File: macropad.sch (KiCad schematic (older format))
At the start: 27 parts

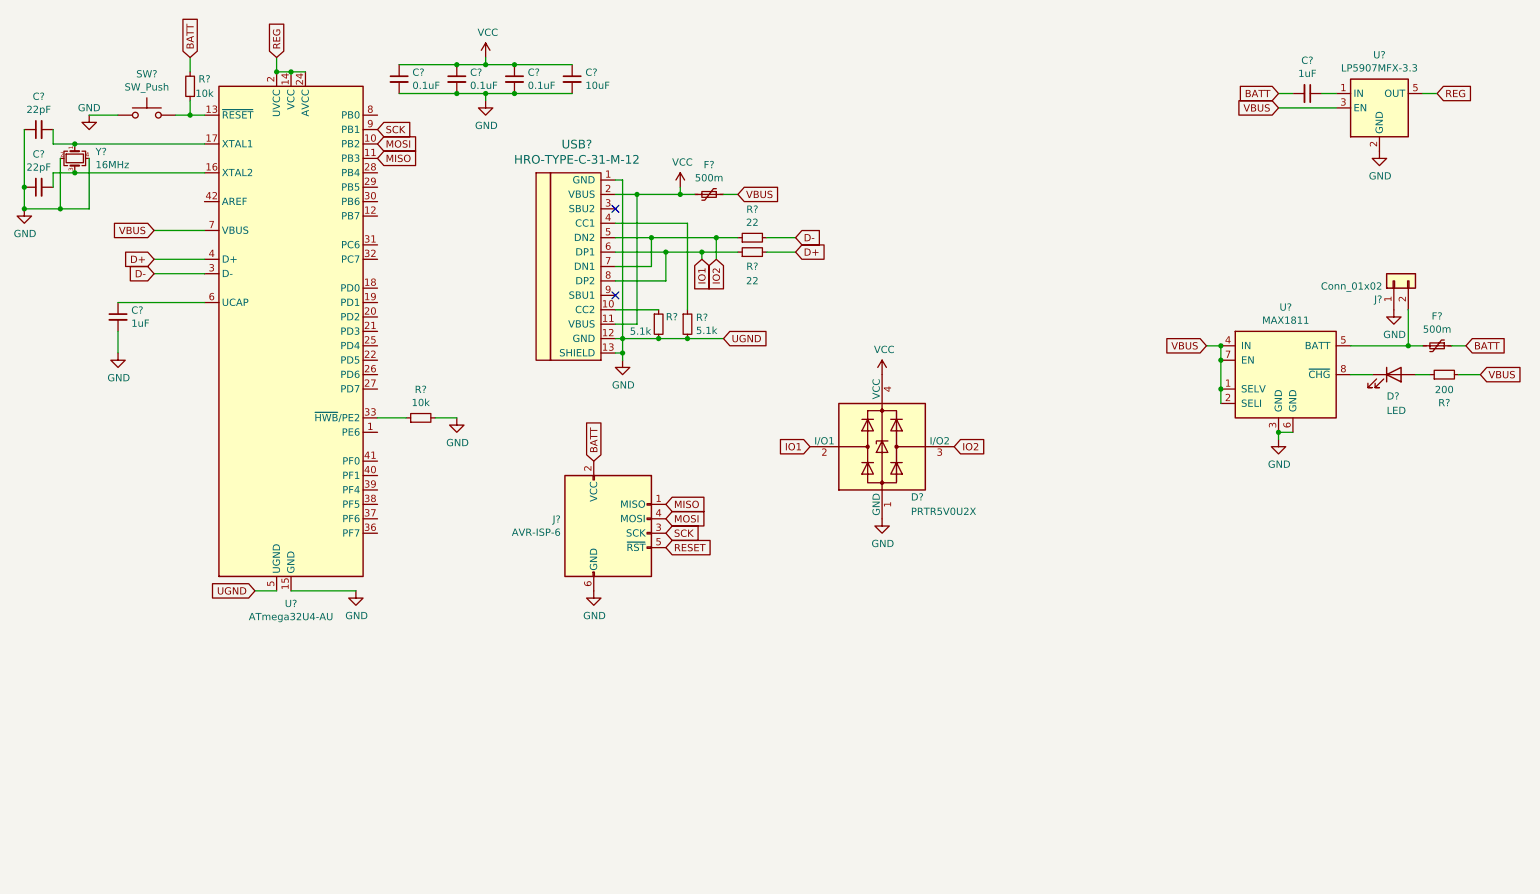
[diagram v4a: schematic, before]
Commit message: Power source switching, hopefully it doesn't explode
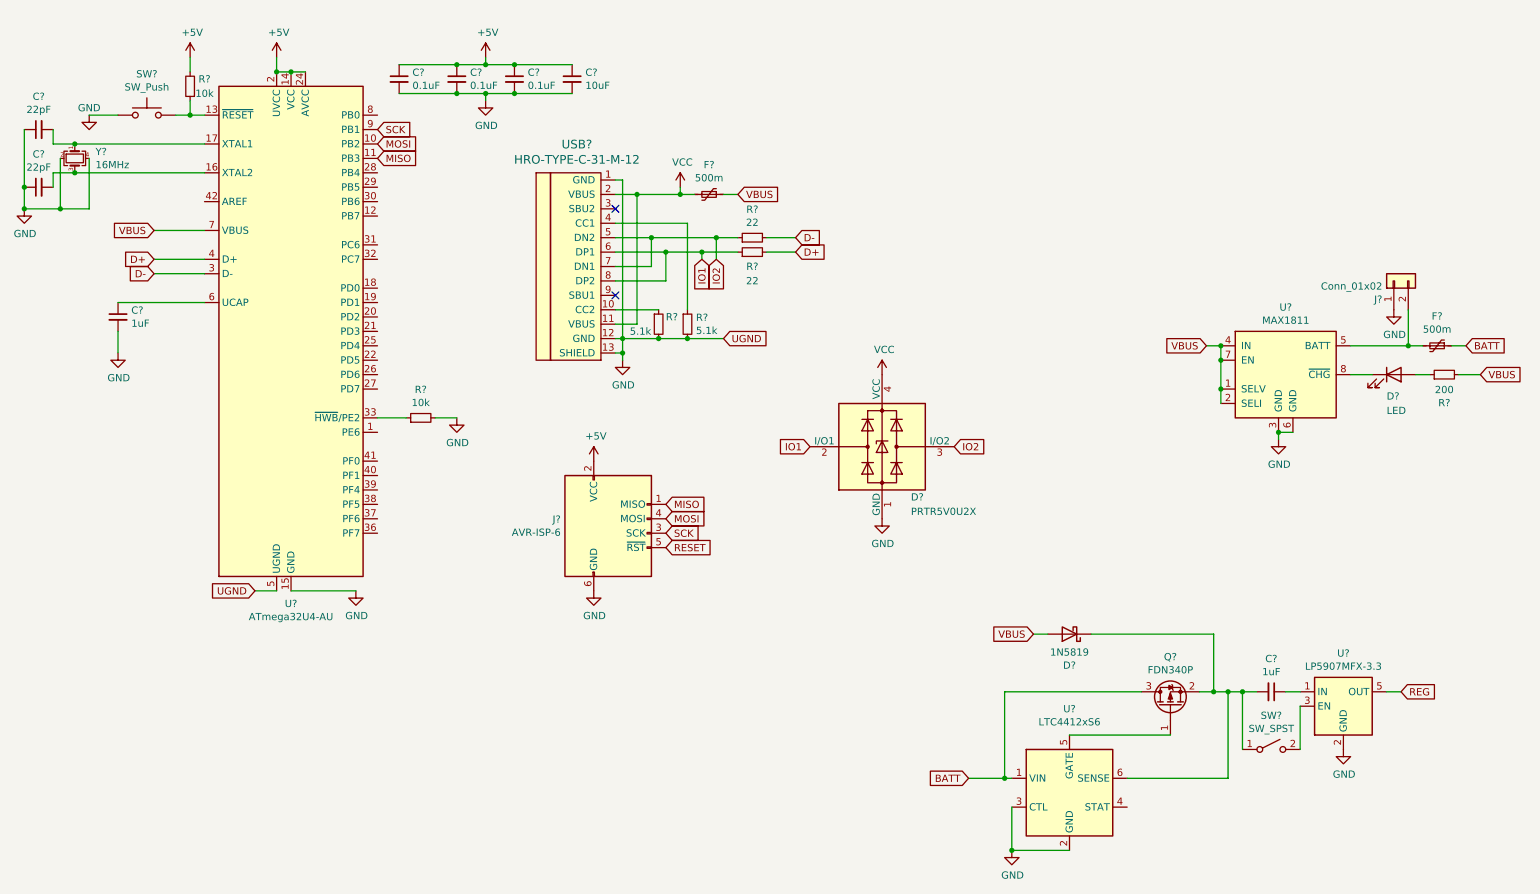
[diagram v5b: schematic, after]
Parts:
- added D?: 1N5819, Diode_THT:D_DO-41_SOD81_P10.16mm_Horizontal, symbol Diode:1N5819
- added Q?: FDN340P, Package_TO_SOT_SMD:SOT-23, symbol Transistor_FET:FDN340P
- added SW?: SW_SPST, symbol Switch:SW_SPST
- added U?: LTC4412xS6, Package_TO_SOT_SMD:TSOT-23-6, symbol Power_Management:LTC4412xS6
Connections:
- net BATT: now also Q?.3 (D), U?.1 (VIN); no longer C?.2, J?.2 (VCC), R?.2
- net GND: now also U?.2 (GND), U?.3 (CTL)
- net REG: no longer U?.14 (VCC), U?.2 (UVCC), U?.24 (AVCC), U?.34 (VCC), U?.44 (AVCC)
- net VBUS: now also D?.2 (A); no longer U?.3 (EN)
- net VCC: no longer C?.1, C?.1, C?.1, C?.1
- new net: SW?.2 (B), U?.3 (EN)
- new net: C?.2, D?.1 (K), Q?.2 (S), SW?.1 (A), U?.6 (SENSE)
- new net: Q?.1 (G), U?.5 (GATE)
- new net +5V: C?.1, C?.1, C?.1, C?.1, J?.2 (VCC), R?.2, U?.14 (VCC), U?.2 (UVCC), U?.24 (AVCC), U?.34 (VCC), U?.44 (AVCC)
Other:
- moved on the sheet: C?, U?
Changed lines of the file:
@@
 	1000 1550 1900 1550
-Wire Wire Line
-	3850 800  4050 800
-Connection ~ 3850 800
-Wire Wire Line
-	3650 800  3850 800
 Wire Wire Line
 	3650 1000 3850 1000
@@
 Wire Wire Line
 	3850 1050 3850 1000
-Wire Wire Line
-	3850 750  3850 800
-$Comp
-L power:VCC #PWR?
-U 1 1 60C49678
-P 3850 750
-F 0 "#PWR?" H 3850 600 50  0001 C CNN
-F 1 "VCC" H 3865 923 50  0000 C CNN
-F 2 "" H 3850 750 50  0001 C CNN
-F 3 "" H 3850 750 50  0001 C CNN
-	1    3850 750
-	1    0    0    -1
-$EndComp
 $Comp
 L Device:C_Small C?
@@
 Text GLabel 5500 2700 2    50   Input ~ 0
 UGND
-Text GLabel 2400 750  1    50   Input ~ 0
-REG
 $Comp
 L Device:R_Small R?
@@
 L Regulator_Linear:LP5907MFX-3.3 U?
 U 1 1 60D4DF09
-P 10050 1100
-F 0 "U?" H 10050 1467 50  0000 C CNN
-F 1 "LP5907MFX-3.3" H 10050 1376 50  0000 C CNN
-F 2 "Package_TO_SOT_SMD:SOT-23-5" H 10050 1450 50  0001 C CNN
-F 3 "http://www.ti.com/lit/ds/symlink/lp5907.pdf" H 10050 1600 50  0001 C CNN
-	1    10050 1100
-	1    0    0    -1
-$EndComp
-Text GLabel 9350 1000 0    50   Input ~ 0
-BATT
-Wire Wire Line
-	9650 1000 9750 1000
+P 9800 5250
+F 0 "U?" H 9800 5617 50  0000 C CNN
+F 1 "LP5907MFX-3.3" H 9800 5526 50  0000 C CNN
+F 2 "Package_TO_SOT_SMD:SOT-23-5" H 9800 5600 50  0001 C CNN
+F 3 "http://www.ti.com/lit/ds/symlink/lp5907.pdf" H 9800 5750 50  0001 C CNN
+	1    9800 5250
+	1    0    0    -1
+$EndComp
+Wire Wire Line
+	9400 5150 9500 5150
 $Comp
 L Device:C_Small C?
 U 1 1 60D5BC90
-P 9550 1000
-F 0 "C?" V 9321 1000 50  0000 C CNN
-F 1 "1uF" V 9412 1000 50  0000 C CNN
-F 2 "" H 9550 1000 50  0001 C CNN
-F 3 "~" H 9550 1000 50  0001 C CNN
-	1    9550 1000
+P 9300 5150
+F 0 "C?" V 9071 5150 50  0000 C CNN
+F 1 "1uF" V 9162 5150 50  0000 C CNN
+F 2 "" H 9300 5150 50  0001 C CNN
+F 3 "~" H 9300 5150 50  0001 C CNN
+	1    9300 5150
 	0    1    1    0
 $EndComp
-Wire Wire Line
-	9350 1000 9450 1000
 $Comp
 L power:GND #PWR?
 U 1 1 60D69A13
-P 10050 1400
-F 0 "#PWR?" H 10050 1150 50  0001 C CNN
-F 1 "GND" H 10055 1227 50  0000 C CNN
-F 2 "" H 10050 1400 50  0001 C CNN
-F 3 "" H 10050 1400 50  0001 C CNN
-	1    10050 1400
-	1    0    0    -1
-$EndComp
-Text GLabel 9350 1100 0    50   Input ~ 0
-VBUS
-Wire Wire Line
-	9350 1100 9750 1100
-Text GLabel 10450 1000 2    50   Input ~ 0
+P 9800 5550
+F 0 "#PWR?" H 9800 5300 50  0001 C CNN
+F 1 "GND" H 9805 5377 50  0000 C CNN
+F 2 "" H 9800 5550 50  0001 C CNN
+F 3 "" H 9800 5550 50  0001 C CNN
+	1    9800 5550
+	1    0    0    -1
+$EndComp
+Text GLabel 10200 5150 2    50   Input ~ 0
 REG
 Wire Wire Line
-	10450 1000 10350 1000
+	10200 5150 10100 5150
 $Comp
 L Battery_Management:MAX1811 U?
@@
 Text GLabel 5100 4150 2    50   Input ~ 0
 RESET
-Text GLabel 4600 3550 1    50   Input ~ 0
-BATT
 $Comp
 L power:GND #PWR?
@@
 Wire Wire Line
 	1700 1150 1800 1150
-Text GLabel 1800 750  1    50   Input ~ 0
-BATT
 Wire Wire Line
 	1800 750  1800 850
@@
 	-1   0    0    1
 $EndComp
+$Comp
+L Power_Management:LTC4412xS6 U?
+U 1 1 60FD7D97
+P 7900 5850
+F 0 "U?" H 7900 6431 50  0000 C CNN
+F 1 "LTC4412xS6" H 7900 6340 50  0000 C CNN
+F 2 "Package_TO_SOT_SMD:TSOT-23-6" H 8550 5500 50  0001 C CNN
+F 3 "https://www.analog.com/media/en/technical-documentation/data-sheets/4412fb.pdf" H 10000 5650 50  0001 C CNN
+	1    7900 5850
+	1    0    0    -1
+$EndComp
+$Comp
+L Diode:1N5819 D?
+U 1 1 60FF6140
+P 7900 4750
+F 0 "D?" H 7900 4967 50  0000 C CNN
+F 1 "1N5819" H 7900 4876 50  0000 C CNN
+F 2 "Diode_THT:D_DO-41_SOD81_P10.16mm_Horizontal" H 7900 4575 50  0001 C CNN
+F 3 "http://www.vishay.com/docs/88525/1n5817.pdf" H 7900 4750 50  0001 C CNN
+	1    7900 4750
+	-1   0    0    1
+$EndComp
+Wire Wire Line
+	3650 800  3850 800
+Wire Wire Line
+	3850 800  3850 750
+Connection ~ 3850 800
+Wire Wire Line
+	3850 800  4050 800
+$Comp
+L Transistor_FET:FDN340P Q?
+U 1 1 610158B0
+P 8600 5250
+F 0 "Q?" V 8942 5250 50  0000 C CNN
+F 1 "FDN340P" V 8851 5250 50  0000 C CNN
+F 2 "Package_TO_SOT_SMD:SOT-23" H 8800 5175 50  0001 L CIN
+F 3 "https://www.onsemi.com/pub/Collateral/FDN340P-D.PDF" H 8600 5250 50  0001 L CNN
+	1    8600 5250
+	0    -1   -1   0
+$EndComp
+$Comp
+L power:+5V #PWR?
+U 1 1 61021E90
+P 2400 750
+F 0 "#PWR?" H 2400 600 50  0001 C CNN
+F 1 "+5V" H 2415 923 50  0000 C CNN
+F 2 "" H 2400 750 50  0001 C CNN
+F 3 "" H 2400 750 50  0001 C CNN
+	1    2400 750
+	1    0    0    -1
+$EndComp
+$Comp
+L power:+5V #PWR?
+U 1 1 610232C4
+P 1800 750
+F 0 "#PWR?" H 1800 600 50  0001 C CNN
+F 1 "+5V" H 1815 923 50  0000 C CNN
+F 2 "" H 1800 750 50  0001 C CNN
+F 3 "" H 1800 750 50  0001 C CNN
+	1    1800 750
+	1    0    0    -1
+$EndComp
+$Comp
+L power:+5V #PWR?
+U 1 1 610277FD
+P 4600 3550
+F 0 "#PWR?" H 4600 3400 50  0001 C CNN
+F 1 "+5V" H 4615 3723 50  0000 C CNN
+F 2 "" H 4600 3550 50  0001 C CNN
+F 3 "" H 4600 3550 50  0001 C CNN
+	1    4600 3550
+	1    0    0    -1
+$EndComp
+$Comp
+L power:+5V #PWR?
+U 1 1 610420AE
+P 3850 750
+F 0 "#PWR?" H 3850 600 50  0001 C CNN
+F 1 "+5V" H 3865 923 50  0000 C CNN
+F 2 "" H 3850 750 50  0001 C CNN
+F 3 "" H 3850 750 50  0001 C CNN
+	1    3850 750
+	1    0    0    -1
+$EndComp
+Text GLabel 7650 4750 0    50   Input ~ 0
+VBUS
+Wire Wire Line
+	7650 4750 7750 4750
+Text GLabel 7200 5750 0    50   Input ~ 0
+BATT
+Wire Wire Line
+	7200 5750 7450 5750
+Wire Wire Line
+	8600 5450 7900 5450
+Wire Wire Line
+	8400 5150 7450 5150
+Wire Wire Line
+	7450 5150 7450 5750
+Connection ~ 7450 5750
+Wire Wire Line
+	7450 5750 7500 5750
+$Comp
+L Switch:SW_SPST SW?
+U 1 1 610B4C5A
+P 9300 5550
+F 0 "SW?" H 9300 5785 50  0000 C CNN
+F 1 "SW_SPST" H 9300 5694 50  0000 C CNN
+F 2 "" H 9300 5550 50  0001 C CNN
+F 3 "~" H 9300 5550 50  0001 C CNN
+	1    9300 5550
+	1    0    0    -1
+$EndComp
+Wire Wire Line
+	9100 5550 9100 5150
+Wire Wire Line
+	8800 5150 8900 5150
+Wire Wire Line
+	8050 4750 8900 4750
+Wire Wire Line
+	8900 4750 8900 5150
+Connection ~ 8900 5150
+Wire Wire Line
+	8900 5150 9000 5150
+$Comp
+L power:GND #PWR?
+U 1 1 610D3F1D
+P 7500 6250
+F 0 "#PWR?" H 7500 6000 50  0001 C CNN
+F 1 "GND" H 7505 6077 50  0000 C CNN
+F 2 "" H 7500 6250 50  0001 C CNN
+F 3 "" H 7500 6250 50  0001 C CNN
+	1    7500 6250
+	1    0    0    -1
+$EndComp
+Wire Wire Line
+	8300 5750 9000 5750
+Wire Wire Line
+	9000 5750 9000 5150
+Wire Wire Line
+	9100 5150 9200 5150
+Wire Wire Line
+	9500 5550 9500 5250
+Wire Wire Line
+	9000 5150 9100 5150
+Connection ~ 9000 5150
+Connection ~ 9100 5150
+Wire Wire Line
+	7900 6250 7500 6250
+Wire Wire Line
+	7500 6250 7500 5950
+Connection ~ 7500 6250
 $EndSCHEMATC
